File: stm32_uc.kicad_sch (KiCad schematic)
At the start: 26 parts

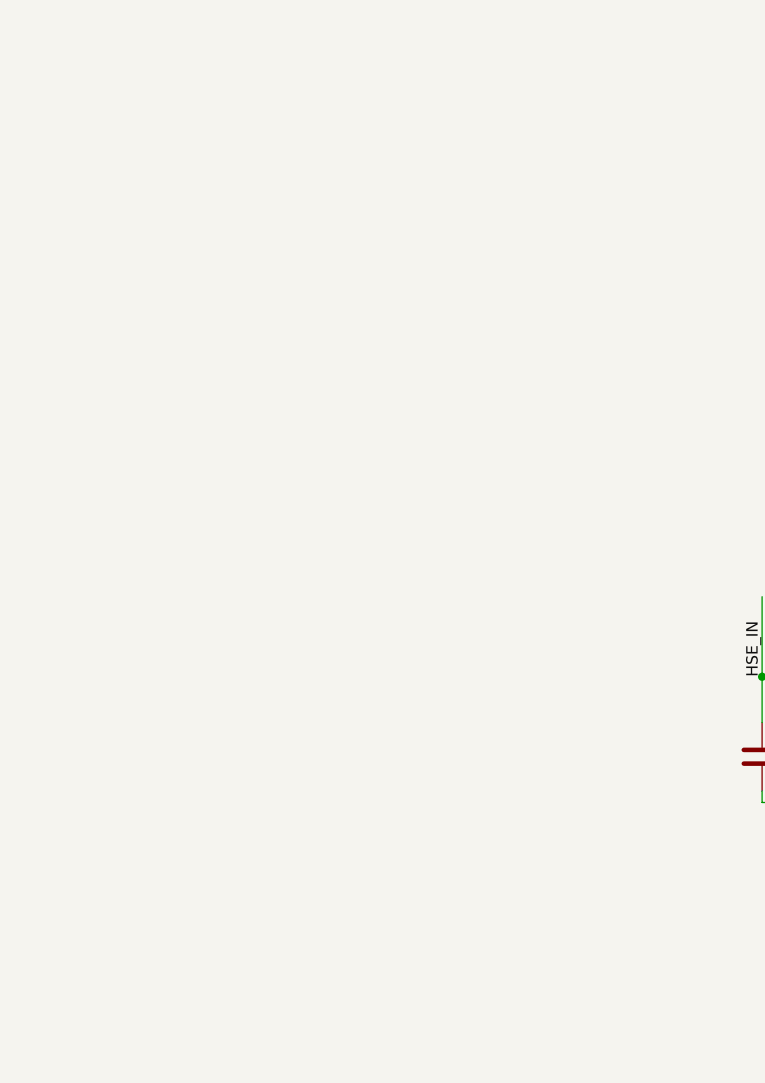
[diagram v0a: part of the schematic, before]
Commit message: started adding connectors
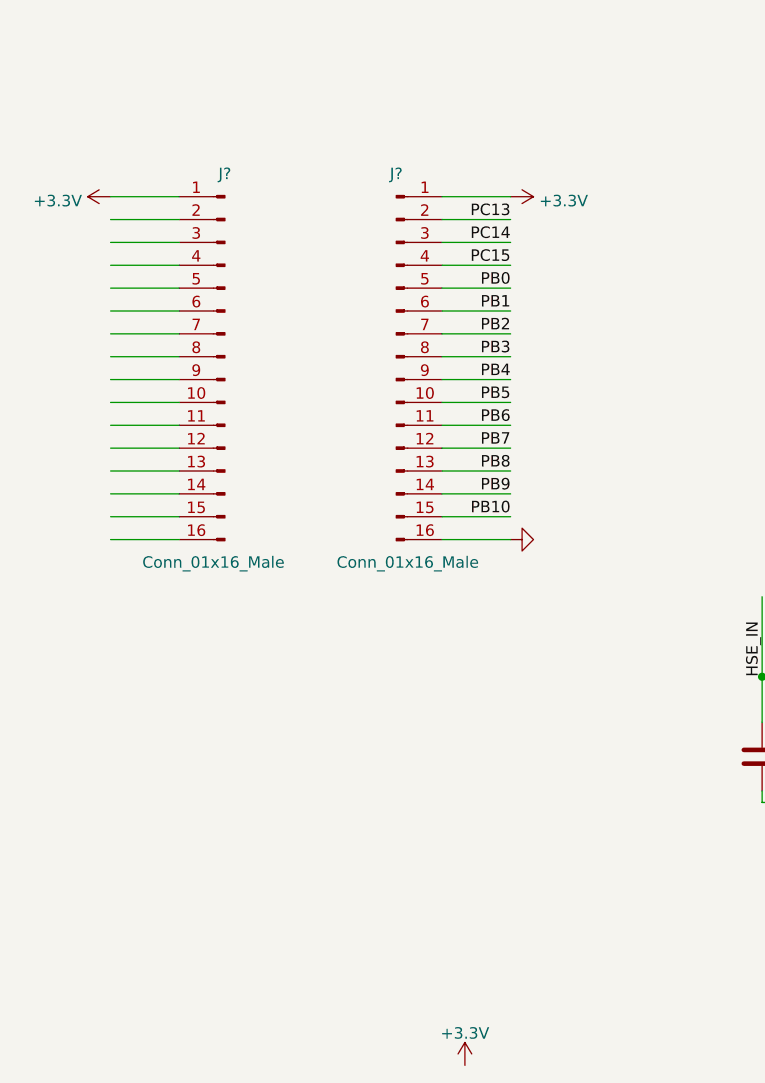
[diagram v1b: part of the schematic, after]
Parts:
- added J? (x2): Conn_01x16_Male, symbol Connector:Conn_01x16_Male
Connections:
- net +3V3: now also J?.1 (Pin_1), J?.1 (Pin_1)
- net GND: now also J?.16 (Pin_16)
- net PB0: now also J?.5 (Pin_5)
- net PB1: now also J?.6 (Pin_6)
- net PB10: now also J?.15 (Pin_15)
- net PB2: now also J?.7 (Pin_7)
- net PB3: now also J?.8 (Pin_8)
- net PB4: now also J?.9 (Pin_9)
- net PB5: now also J?.10 (Pin_10)
- net PB6: now also J?.11 (Pin_11)
- net PB7: now also J?.12 (Pin_12)
- net PB8: now also J?.13 (Pin_13)
- net PB9: now also J?.14 (Pin_14)
- net PC13: now also J?.2 (Pin_2)
- net PC14: now also J?.3 (Pin_3)
- net PC15: now also J?.4 (Pin_4)

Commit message: finished connectors
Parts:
- removed J? (x2): Conn_01x16_Male, symbol Connector:Conn_01x16_Male
- added J? (x2): Conn_01x18_Male, symbol Connector:Conn_01x18_Male
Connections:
- net PC13 is gone; now on net +3V3: U?.2 (PC13)
- net +3V3: now also J?.1 (Pin_1), J?.1 (Pin_1), J?.2 (Pin_2), J?.3 (Pin_3)
- net GND: now also J?.17 (Pin_17), J?.18 (Pin_18), J?.18 (Pin_18)
- net PA0: now also J?.7 (Pin_7)
- net PA1: now also J?.8 (Pin_8)
- net PA15: now also J?.17 (Pin_17)
- net PA2: now also J?.9 (Pin_9)
- net PA3: now also J?.10 (Pin_10)
- net PA4: now also J?.11 (Pin_11)
- net PA5: now also J?.12 (Pin_12)
- net PA6: now also J?.13 (Pin_13)
- net PA7: now also J?.14 (Pin_14)
- net PA8: now also J?.15 (Pin_15)
- net PA9: now also J?.16 (Pin_16)
- net PB0: now also J?.6 (Pin_6)
- net PB1: now also J?.7 (Pin_7)
- net PB10: now also J?.16 (Pin_16)
- net PB11: now also J?.2 (Pin_2)
- net PB12: now also J?.3 (Pin_3)
- net PB13: now also J?.4 (Pin_4)
- net PB14: now also J?.5 (Pin_5)
- net PB15: now also J?.6 (Pin_6)
- net PB2: now also J?.8 (Pin_8)
- net PB3: now also J?.9 (Pin_9)
- net PB4: now also J?.10 (Pin_10)
- net PB5: now also J?.11 (Pin_11)
- net PB6: now also J?.12 (Pin_12)
- net PB7: now also J?.13 (Pin_13)
- net PB8: now also J?.14 (Pin_14)
- net PB9: now also J?.15 (Pin_15)
- net PC14: now also J?.4 (Pin_4)
- net PC15: now also J?.5 (Pin_5)

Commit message: started anotating schematic
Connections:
- net USB_D+: no longer J?.A6 (D+), J?.B6 (D+), R?.2
- net USB_D-: no longer J?.A7 (D-), J?.B7 (D-)
- new net: J?.A6 (D+), J?.B6 (D+), R?.2
- new net: J?.A7 (D-), J?.B7 (D-)
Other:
- moved on the sheet: C?, D?, FB?, J?, R?, SW?, U?, Y?
